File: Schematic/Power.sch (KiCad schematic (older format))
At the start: 18 parts, among them U5 MCP73812T-420I-OT, U6 STC3100IST, U7 MIC5504-3.3YM5, U8 MIC5504-3.3YM5

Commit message: Add passives
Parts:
- added C?: 100nF, symbol Device:C
- added D?: LED, symbol Device:LED
- added R?: R, symbol Device:R
- C?: value C -> 100nF
- R?: value R -> 10m
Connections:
- net GND: now also C?.2, R?.2
- net at D?.2 (A), D?.2 (A), J?.1 (VBUS): now also C?.1
- new net: D?.1 (K), R?.1
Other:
- moved on the sheet: BT?, C?, D?, J?, R?, U5, U6, U7, U8

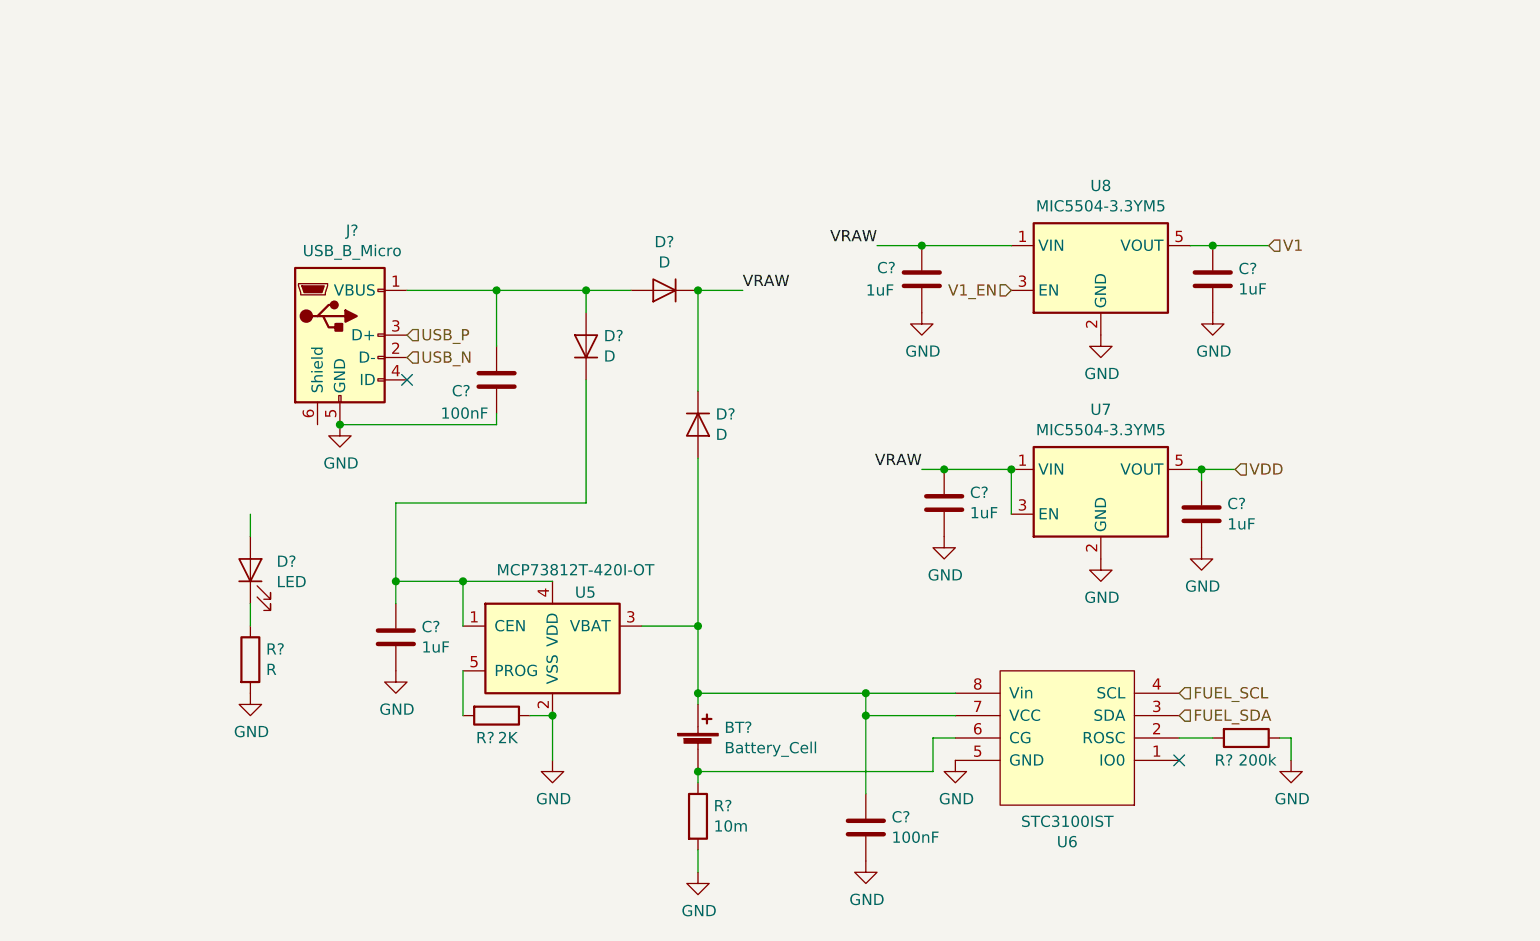
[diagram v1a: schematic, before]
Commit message: Perform annotation start assigning footprints
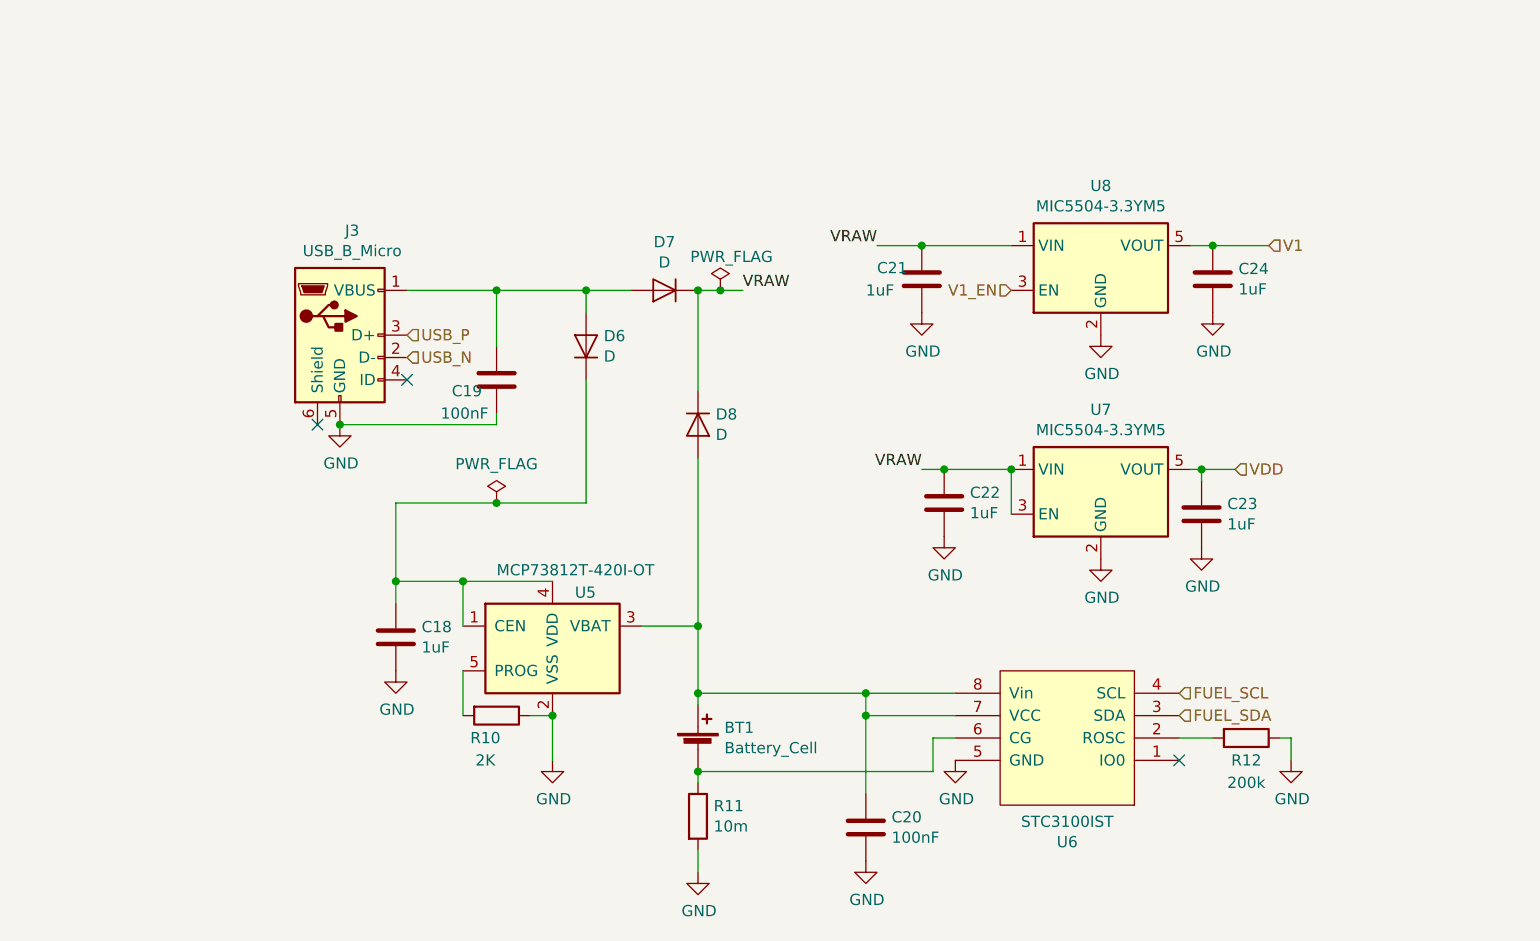
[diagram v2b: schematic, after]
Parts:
- removed D?: LED, symbol Device:LED
- removed R?: R, symbol Device:R
- C18, C19, C20, C21, C22, C23, C24: renamed from C?; footprint (none) -> Capacitor_SMD:C_0603_1608Metric_Pad1.05x0.95mm_HandSolder
- D6, D7, D8: renamed from D?; footprint (none) -> Diode_SMD:D_0603_1608Metric_Pad1.05x0.95mm_HandSolder
- R10, R11, R12: renamed from R?; footprint (none) -> Resistor_SMD:R_0603_1608Metric_Pad1.05x0.95mm_HandSolder
- gave numbers to parts that had none: 2
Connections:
- no-connect marks 2 -> 3

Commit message: Selected components
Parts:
- removed D6, D7, D8: D, Diode_SMD:D_0603_1608Metric_Pad1.05x0.95mm_HandSolder, symbol Device:D
- added D5, D6, D7: D_Schottky, Diode_SMD:D_0603_1608Metric_Pad1.05x0.95mm_HandSolder, symbol Device:D_Schottky
- BT1: footprint (none) -> Connector_JST:JST_PH_B2B-PH-K_1x02_P2.00mm_Vertical
- J3: footprint (none) -> Connector_USB:USB_Micro-B_Amphenol_10103594-0001LF_Horizontal
- U6: footprint (none) -> Package_SO:MSOP-8_3x3mm_P0.65mm
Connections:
- net VRAW: now also D5.1 (K), D7.1 (K)
- net at BT1.1 (+), C20.1, U5.3 (VBAT)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: now also D5.2 (A)
- net at C18.1, U5.1 (CEN), U5.4 (VDD): now also D6.1 (K)
- net at C19.1, J3.1 (VBUS): now also D6.2 (A), D7.2 (A)
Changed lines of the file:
@@
 EESchema Schematic File Version 4
-LIBS:SoundBoard-cache
-EELAYER 26 0
+EELAYER 30 0
 EELAYER END
 $Descr A4 11693 8268
@@
 F 0 "U6" H 5700 4665 50  0000 C CNN
 F 1 "STC3100IST" H 5700 4574 50  0000 C CNN
-F 2 "" H 5700 4450 50  0001 C CNN
+F 2 "Package_SO:MSOP-8_3x3mm_P0.65mm" H 5700 4450 50  0001 C CNN
 F 3 "" H 5700 4450 50  0001 C CNN
 	1    5700 4450
@@
 $EndComp
 $Comp
-L Device:Battery_Cell BT1
-U 1 1 5E27C1DA
-P 4050 4250
-F 0 "BT1" H 4168 4346 50  0000 L CNN
-F 1 "Battery_Cell" H 4168 4255 50  0000 L CNN
-F 2 "" V 4050 4310 50  0001 C CNN
-F 3 "~" V 4050 4310 50  0001 C CNN
-	1    4050 4250
-	1    0    0    -1
-$EndComp
-$Comp
 L power:GND #PWR0101
 U 1 1 5E27C27E
@@
 	4050 4400 4050 4350
 $Comp
-L Device:D D8
-U 1 1 5E27C7ED
-P 4050 2800
-F 0 "D8" V 4004 2879 50  0000 L CNN
-F 1 "D" V 4095 2879 50  0000 L CNN
-F 2 "Diode_SMD:D_0603_1608Metric_Pad1.05x0.95mm_HandSolder" H 4050 2800 50  0001 C CNN
-F 3 "~" H 4050 2800 50  0001 C CNN
-	1    4050 2800
-	0    1    1    0
-$EndComp
-$Comp
 L power:GND #PWR0102
 U 1 1 5E27C911
@@
 F 0 "J3" H 2505 2867 50  0000 C CNN
 F 1 "USB_B_Micro" H 2505 2776 50  0000 C CNN
-F 2 "" H 2600 2350 50  0001 C CNN
+F 2 "Connector_USB:USB_Micro-B_Amphenol_10103594-0001LF_Horizontal" H 2600 2350 50  0001 C CNN
 F 3 "~" H 2600 2350 50  0001 C CNN
 	1    2450 2400
@@
 Wire Wire Line
 	4050 4700 4050 4800
-Connection ~ 4050 4350
 Connection ~ 4050 4000
 Wire Wire Line
@@
 	4050 3700 4050 2950
 NoConn ~ 6200 4300
-$Comp
-L Device:D D6
-U 1 1 5E28FE3D
-P 3550 2450
-F 0 "D6" V 3596 2371 50  0000 R CNN
-F 1 "D" V 3505 2371 50  0000 R CNN
-F 2 "Diode_SMD:D_0603_1608Metric_Pad1.05x0.95mm_HandSolder" H 3550 2450 50  0001 C CNN
-F 3 "~" H 3550 2450 50  0001 C CNN
-	1    3550 2450
-	0    -1   -1   0
-$EndComp
 Text HLabel 6200 4100 2    50   Input ~ 0
 FUEL_SDA
@@
 	2750 2200 3150 2200
 $Comp
-L Device:D D7
-U 1 1 5E27C710
-P 3900 2200
-F 0 "D7" H 3900 1984 50  0000 C CNN
-F 1 "D" H 3900 2075 50  0000 C CNN
-F 2 "Diode_SMD:D_0603_1608Metric_Pad1.05x0.95mm_HandSolder" H 3900 2200 50  0001 C CNN
-F 3 "~" H 3900 2200 50  0001 C CNN
-	1    3900 2200
-	-1   0    0    1
-$EndComp
-$Comp
 L Device:C C19
 U 1 1 5E2B75E3
@@
 	3150 2200 3550 2200
 Connection ~ 3550 2200
-Wire Wire Line
-	4050 2200 4050 2650
-Connection ~ 4050 2200
 Wire Wire Line
 	2700 3150 2700 3500
@@
 Text Label 4850 2000 2    50   ~ 0
 VRAW
-$Comp
-L power:PWR_FLAG #FLG0101
-U 1 1 5E466669
-P 4150 2200
-F 0 "#FLG0101" H 4150 2275 50  0001 C CNN
-F 1 "PWR_FLAG" H 4200 2350 50  0000 C CNN
-F 2 "" H 4150 2200 50  0001 C CNN
-F 3 "~" H 4150 2200 50  0001 C CNN
-	1    4150 2200
-	1    0    0    -1
-$EndComp
 Wire Wire Line
 	4150 2200 4050 2200
 Connection ~ 4150 2200
-Wire Wire Line
-	4250 2200 4150 2200
 Text Label 4250 2200 0    50   ~ 0
 VRAW
@@
 Wire Wire Line
 	3150 3150 3550 3150
+Connection ~ 4050 4350
+$Comp
+L Device:Battery_Cell BT1
+U 1 1 5E27C1DA
+P 4050 4250
+F 0 "BT1" H 4168 4346 50  0000 L CNN
+F 1 "Battery_Cell" H 4168 4255 50  0000 L CNN
+F 2 "Connector_JST:JST_PH_B2B-PH-K_1x02_P2.00mm_Vertical" V 4050 4310 50  0001 C CNN
+F 3 "~" V 4050 4310 50  0001 C CNN
+	1    4050 4250
+	1    0    0    -1
+$EndComp
+$Comp
+L Device:D_Schottky D5
+U 1 1 5E3095AE
+P 4050 2800
+F 0 "D5" V 4004 2879 50  0000 L CNN
+F 1 "D_Schottky" V 4095 2879 50  0000 L CNN
+F 2 "Diode_SMD:D_0603_1608Metric_Pad1.05x0.95mm_HandSolder" H 4050 2800 50  0001 C CNN
+F 3 "~" H 4050 2800 50  0001 C CNN
+	1    4050 2800
+	0    1    1    0
+$EndComp
+$Comp
+L Device:D_Schottky D7
+U 1 1 5E30E3ED
+P 3900 2200
+F 0 "D7" H 3900 1984 50  0000 C CNN
+F 1 "D_Schottky" H 3900 2075 50  0000 C CNN
+F 2 "Diode_SMD:D_0603_1608Metric_Pad1.05x0.95mm_HandSolder" H 3900 2200 50  0001 C CNN
+F 3 "~" H 3900 2200 50  0001 C CNN
+	1    3900 2200
+	-1   0    0    1
+$EndComp
+$Comp
+L Device:D_Schottky D6
+U 1 1 5E30FCFE
+P 3550 2450
+F 0 "D6" V 3596 2371 50  0000 R CNN
+F 1 "D_Schottky" V 3505 2371 50  0000 R CNN
+F 2 "Diode_SMD:D_0603_1608Metric_Pad1.05x0.95mm_HandSolder" H 3550 2450 50  0001 C CNN
+F 3 "~" H 3550 2450 50  0001 C CNN
+	1    3550 2450
+	0    -1   -1   0
+$EndComp
+Connection ~ 4050 2200
+Wire Wire Line
+	4250 2200 4150 2200
+$Comp
+L power:PWR_FLAG #FLG0101
+U 1 1 5E466669
+P 4150 2200
+F 0 "#FLG0101" H 4150 2275 50  0001 C CNN
+F 1 "PWR_FLAG" H 4300 2350 50  0000 C CNN
+F 2 "" H 4150 2200 50  0001 C CNN
+F 3 "~" H 4150 2200 50  0001 C CNN
+	1    4150 2200
+	1    0    0    -1
+$EndComp
+Wire Wire Line
+	4050 2200 4050 2650
 $EndSCHEMATC
